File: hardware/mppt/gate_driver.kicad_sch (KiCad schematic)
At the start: 28 parts, among them Q1001 Q_NMOS_GDS, U1001 ADUM4221-1ARIZ

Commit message: placement of majority of power path
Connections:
- net GND: no longer D1002.2 (A), R1003.2
- net GNDPWR: now also D1002.2 (A), R1003.2
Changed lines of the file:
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@@
 	)
 	(junction
-		(at 50.8 68.58)
+		(at 120.65 119.38)
 		(diameter 0)
 		(color 0 0 0 0)
 	)
 	(junction
-		(at 151.13 111.76)
+		(at 50.8 68.58)
 		(diameter 0)
 		(color 0 0 0 0)
 	)
 	(junction
-		(at 130.81 78.74)
+		(at 151.13 111.76)
 		(diameter 0)
 		(color 0 0 0 0)
 	)
 	(junction
-		(at 92.71 93.98)
+		(at 130.81 78.74)
 		(diameter 0)
 		(color 0 0 0 0)
 	)
 	(junction
-		(at 120.65 119.38)
+		(at 92.71 93.98)
 		(diameter 0)
 		(color 0 0 0 0)
@@
 	)
 	(symbol
-		(lib_id "power:GND")
-		(at 120.65 119.38 0)
-		(unit 1)
-		(exclude_from_sim no)
-		(in_bom yes)
-		(on_board yes)
-		(dnp no)
-		(property "Reference" "#PWR01008"
-			(at 120.65 125.73 0)
-			(effects
-				(font
-					(size 1.27 1.27)
-				)
-				(hide yes)
-			)
-		)
-		(property "Value" "GND"
-			(at 120.65 123.698 0)
-			(effects
-				(font
-					(size 1.27 1.27)
-				)
-			)
-		)
-		(property "Footprint" ""
-			(at 120.65 119.38 0)
-			(effects
-				(font
-					(size 1.27 1.27)
-				)
-				(hide yes)
-			)
-		)
-		(property "Datasheet" ""
-			(at 120.65 119.38 0)
-			(effects
-				(font
-					(size 1.27 1.27)
-				)
-				(hide yes)
-			)
-		)
-		(property "Description" "Power symbol creates a global label with name \"GND\" , ground"
-			(at 120.65 119.38 0)
-			(effects
-				(font
-					(size 1.27 1.27)
-				)
-				(hide yes)
-			)
-		)
-		(property "Sim.Device" ""
-			(at 120.65 119.38 0)
-			(effects
-				(font
-					(size 1.27 1.27)
-				)
-				(hide yes)
-			)
-		)
-		(property "Sim.Pins" ""
-			(at 120.65 119.38 0)
-			(effects
-				(font
-					(size 1.27 1.27)
-				)
-				(hide yes)
-			)
-		)
-		(pin "1"
-		)
-		(instances
-			(project "mppt"
-				(path "/83ad0d2f-976b-4ec4-beba-98e6b6988069/1e7e948a-199f-4420-b7b6-1130e9474bfe/6fd27594-6b47-4401-bb7d-37a86a40ba18"
-					(reference "#PWR01008")
-					(unit 1)
-				)
-			)
-		)
-	)
-	(symbol
 		(lib_id "Device:D_Zener_Small")
 		(at 151.13 115.57 270)
@@
 					(unit 1)
 				)
+			)
+		)
+	)
+	(symbol
+		(lib_id "power:GNDPWR")
+		(at 120.65 119.38 0)
+		(unit 1)
+		(exclude_from_sim no)
+		(in_bom yes)
+		(on_board yes)
+		(dnp no)
+		(fields_autoplaced yes)
+		(property "Reference" "#PWR01008"
+			(at 120.65 124.46 0)
+			(effects
+				(font
+					(size 1.27 1.27)
+				)
+				(hide yes)
+			)
+		)
+		(property "Value" "GNDPWR"
+			(at 120.523 123.19 0)
+			(effects
+				(font
+					(size 1.27 1.27)
+				)
+			)
+		)
+		(property "Footprint" ""
+			(at 120.65 120.65 0)
+			(effects
+				(font
+					(size 1.27 1.27)
+				)
+				(hide yes)
+			)
+		)
+		(property "Datasheet" ""
+			(at 120.65 120.65 0)
+			(effects
+				(font
+					(size 1.27 1.27)
+				)
+				(hide yes)
+			)
+		)
+		(property "Description" "Power symbol creates a global label with name \"GNDPWR\" , global ground"
+			(at 120.65 119.38 0)
+			(effects
+				(font
+					(size 1.27 1.27)
+				)
+				(hide yes)
+			)
+		)
+		(property "Sim.Device" ""
+			(at 120.65 119.38 0)
+			(effects
+				(font
+					(size 1.27 1.27)
+				)
+				(hide yes)
+			)
+		)
+		(property "Sim.Pins" ""
+			(at 120.65 119.38 0)
+			(effects
+				(font
+					(size 1.27 1.27)
+				)
+				(hide yes)
+			)
+		)
+		(pin "1"
+		)
+		(instances
+			(project "mppt"
+				(path "/83ad0d2f-976b-4ec4-beba-98e6b6988069/1e7e948a-199f-4420-b7b6-1130e9474bfe/6fd27594-6b47-4401-bb7d-37a86a40ba18"
+					(reference "#PWR01008")
+					(unit 1)
+				)

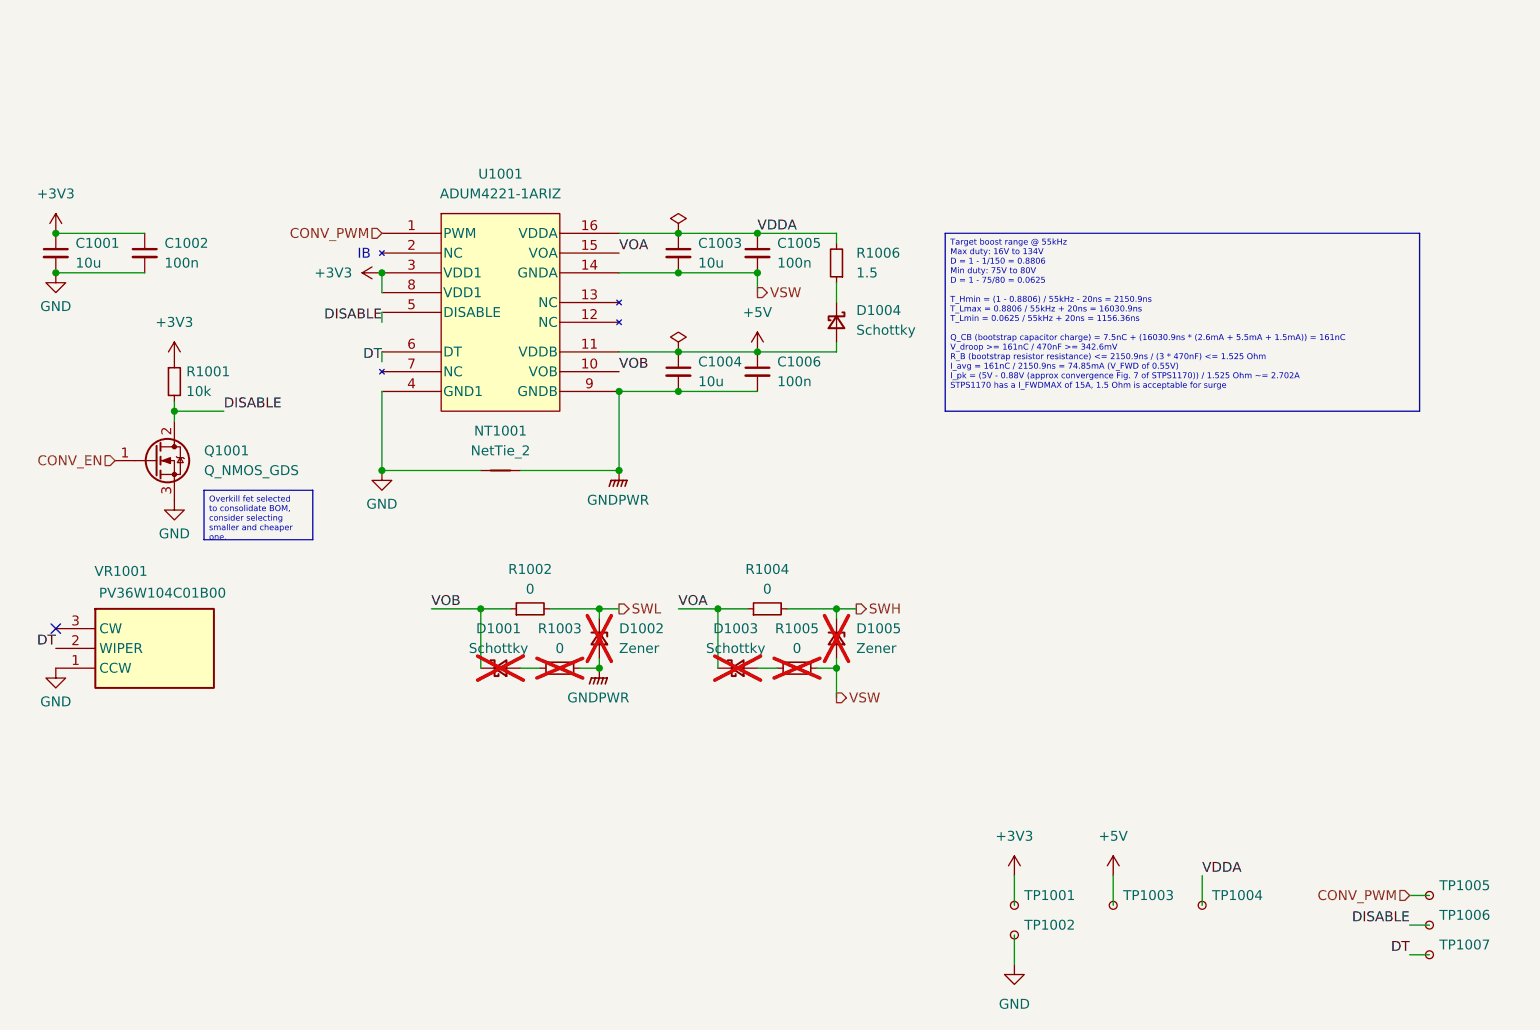
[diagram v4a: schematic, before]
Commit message: PCB variant for power regulation breakout.
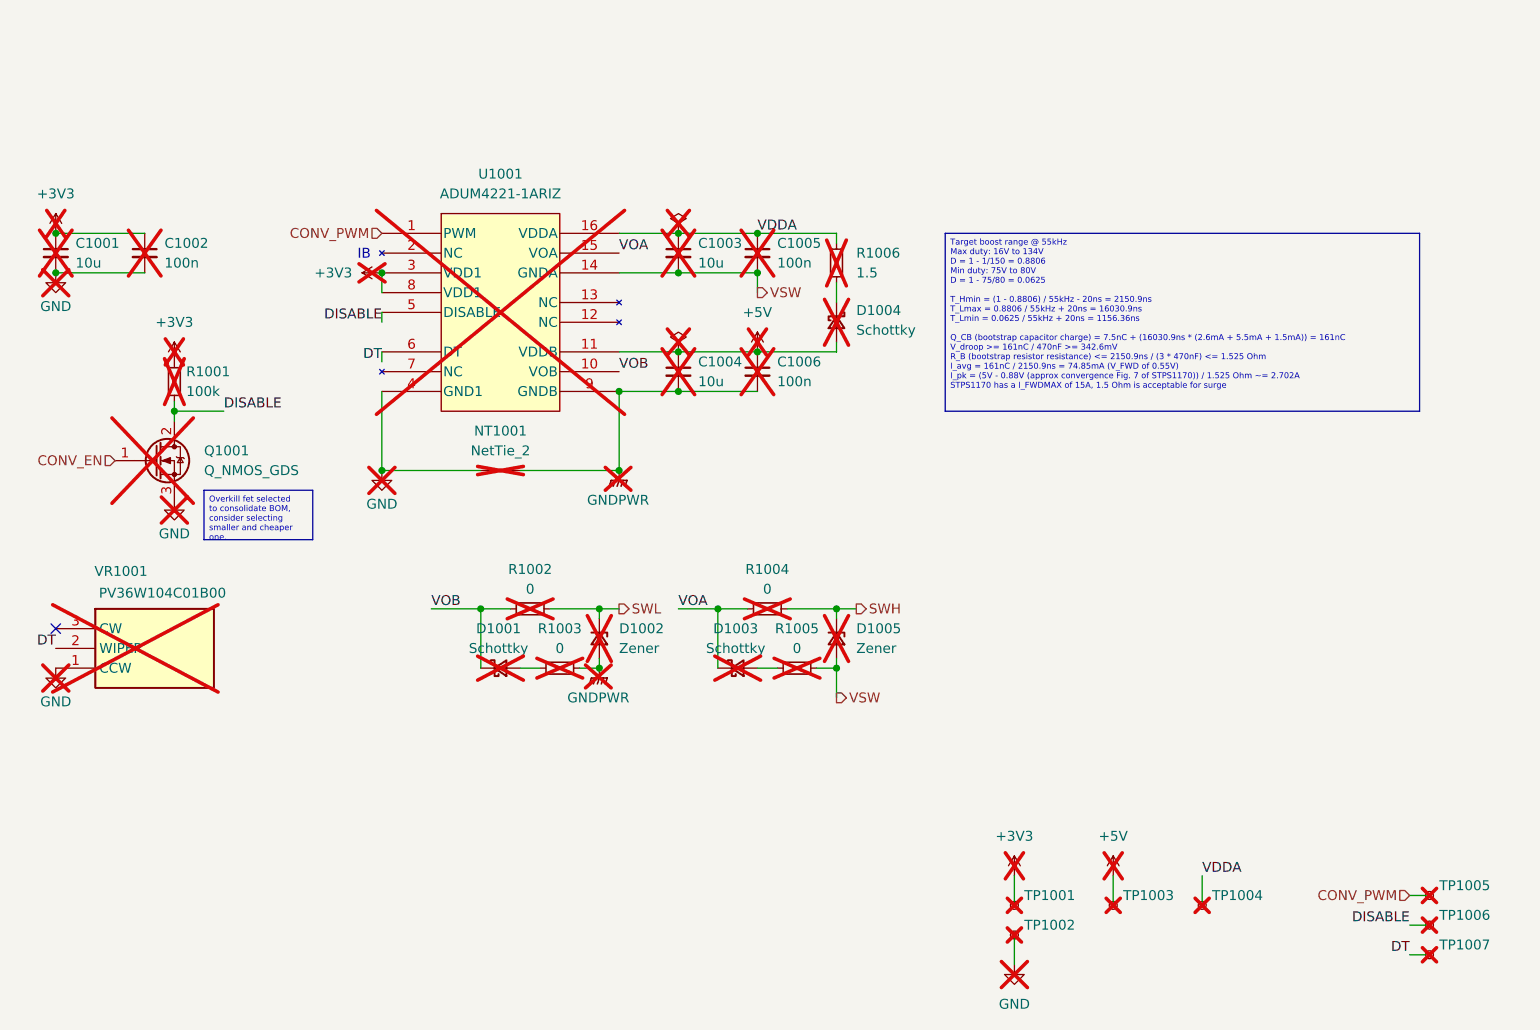
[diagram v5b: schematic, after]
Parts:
- C1001, C1002, C1003, C1004, C1005, C1006, D1004, Q1001, R1002, R1004, R1006, TP1001, TP1002, TP1003, TP1004, TP1005, TP1006, TP1007, U1001, VR1001: now not fitted; now left out of the parts list
- D1001, D1002, D1003, D1005, R1003, R1005: now left out of the parts list
- NT1001: now not fitted; now in the parts list
- R1001: value 10k -> 100k; P/N CRCW060310K0FKEA -> CRCW0603100KFKEA; now not fitted; now left out of the parts list

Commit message: converter schematic and layout.
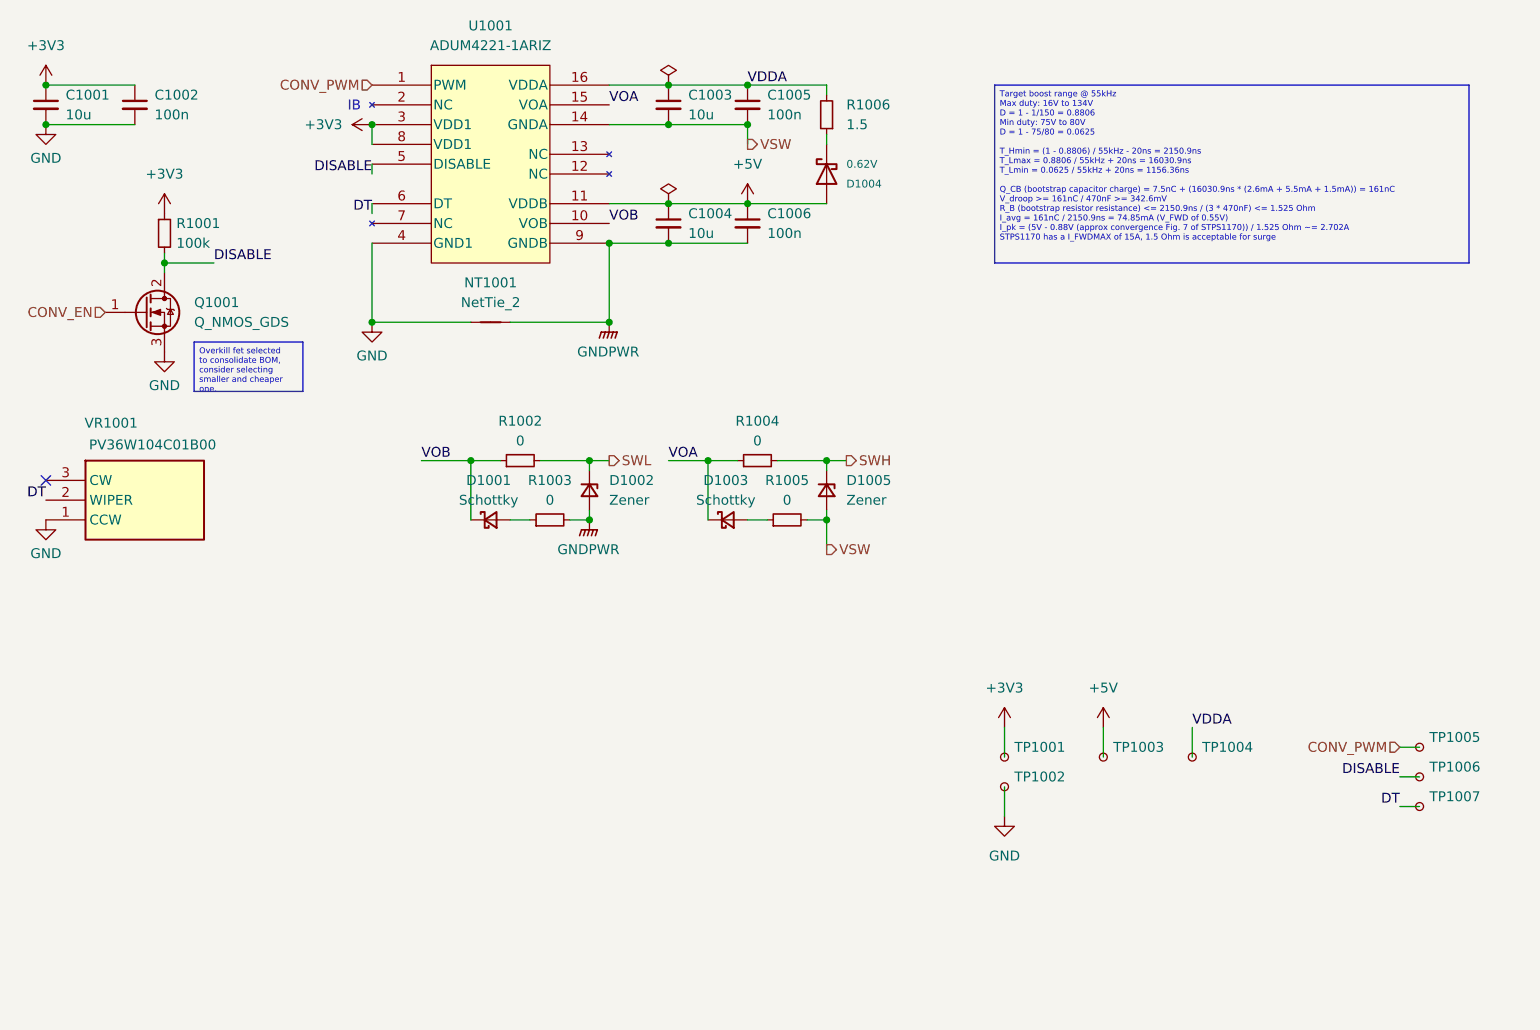
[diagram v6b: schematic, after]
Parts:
- removed D1004: Schottky, Diode_SMD:D_SOD-123F, symbol Device:D_Schottky_Small
- added D1004: 0.62V, Diode_SMD:D_SMA, symbol Device:D_Schottky
- C1001, C1002, C1003, C1004, C1005, C1006, D1001, D1002, D1003, D1005, Q1001, R1001, R1006, TP1001, TP1002, TP1003, TP1004, TP1005, TP1006, TP1007, U1001, VR1001: now fitted; now in the parts list
- NT1001: now fitted
- R1002, R1003, R1004, R1005: footprint Resistor_SMD:R_1210_3225Metric_Pad1.30x2.65mm_HandSolder -> Resistor_SMD:R_0805_2012Metric_Pad1.20x1.40mm_HandSolder; P/N CRCW12100000Z0EA -> CRCW08050000Z0EAHP; now fitted; now in the parts list
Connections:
- net +5V: now also D1004.2 (A)
- net at R1006.1: now also D1004.1 (K)

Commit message: remove testpoints, integrat 60% of layout
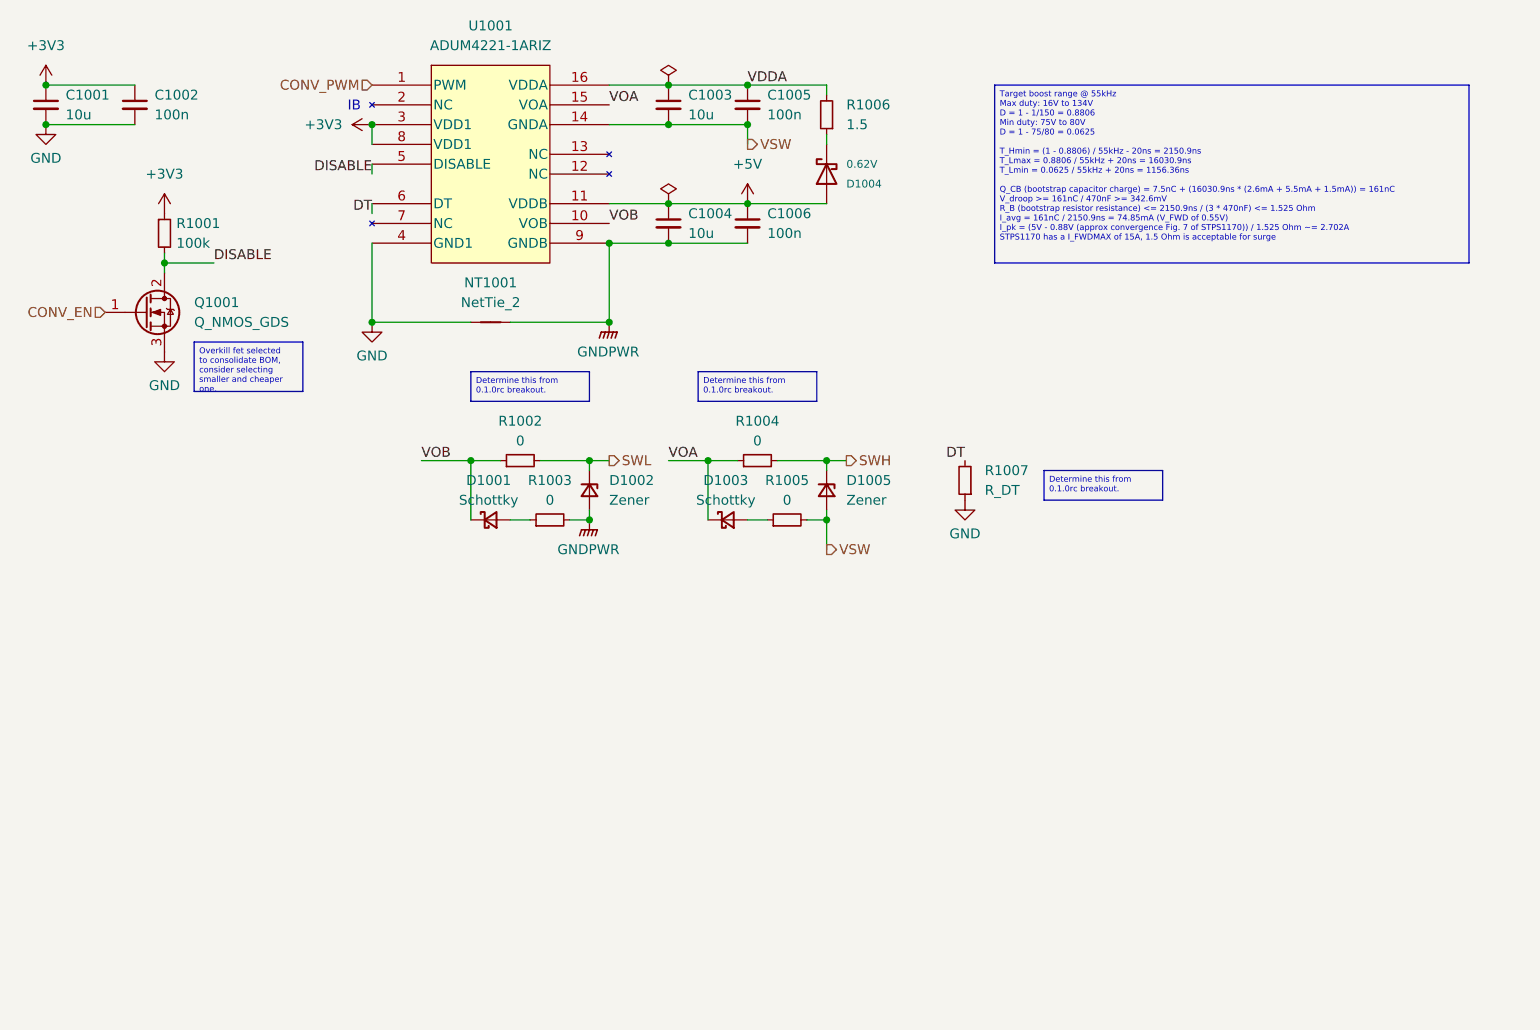
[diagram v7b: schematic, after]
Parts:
- removed TP1001, TP1002, TP1003, TP1004, TP1005, TP1006, TP1007: TestPoint_Small, TestPoint:TestPoint_Pad_D1.0mm, symbol Connector:TestPoint_Small
- removed VR1001: PV36W104C01B00, footprints:bourns_PV36W201C01B00, symbol bourns_PV36W104C01B00:PV36W104C01B00
- added R1007: R_DT, Resistor_SMD:R_0805_2012Metric_Pad1.20x1.40mm_HandSolder, symbol Device:R_Small
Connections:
- net DT: now also R1007.2
- net GND: now also R1007.1
- no-connect marks 1 -> 0
